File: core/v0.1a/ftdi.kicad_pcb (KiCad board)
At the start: 2 copper layers, 32 x 26 mm, 35 parts, among them J1 Conn, P1 pkl_USB_OTG, P2 UP, P3 UP, P4 UP, P5 UP, U1 93C46B-SOT-23-6, U2 FT232H, X1 12MHz

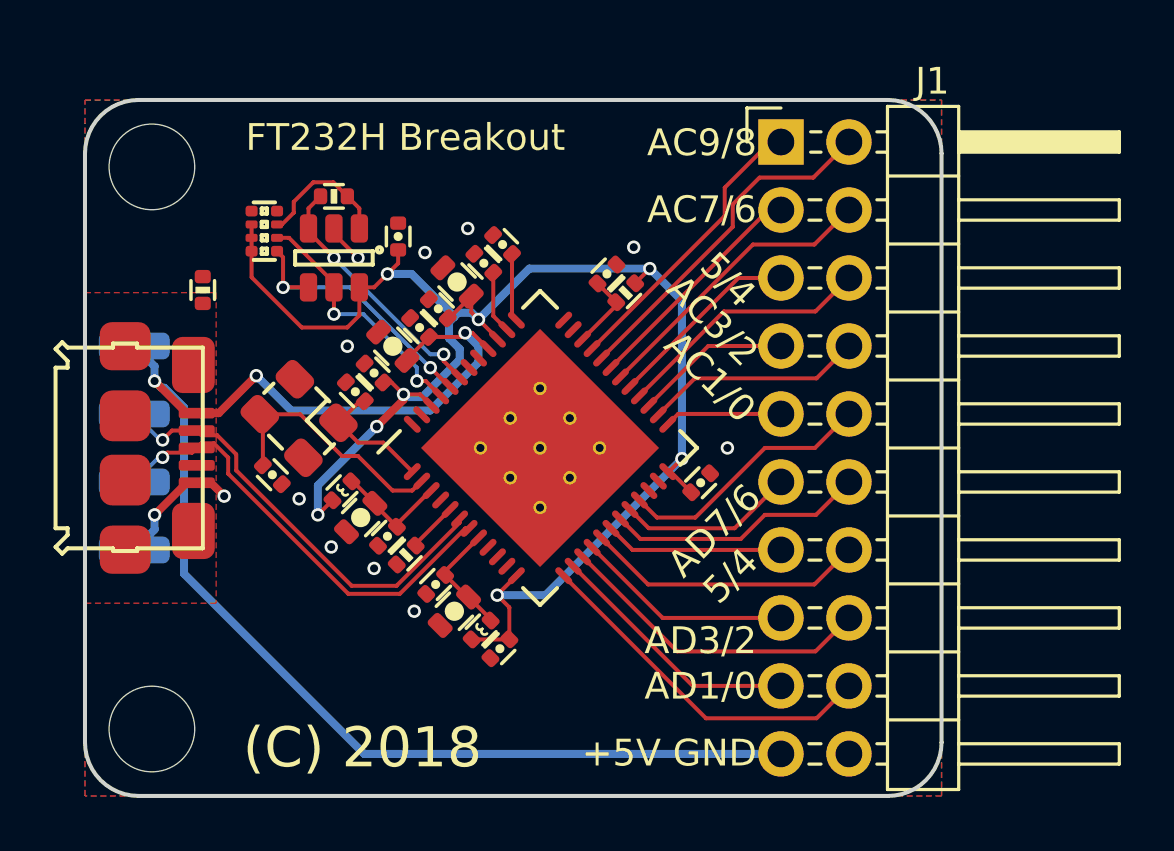
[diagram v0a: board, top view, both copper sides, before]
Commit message: Changed the ftdi breakout design to use a 50mil header.
This also decreases the width of the breakout, which will allow us to
make standard complient 0.8" wide PMOD modules using the breakout board
as a basis.
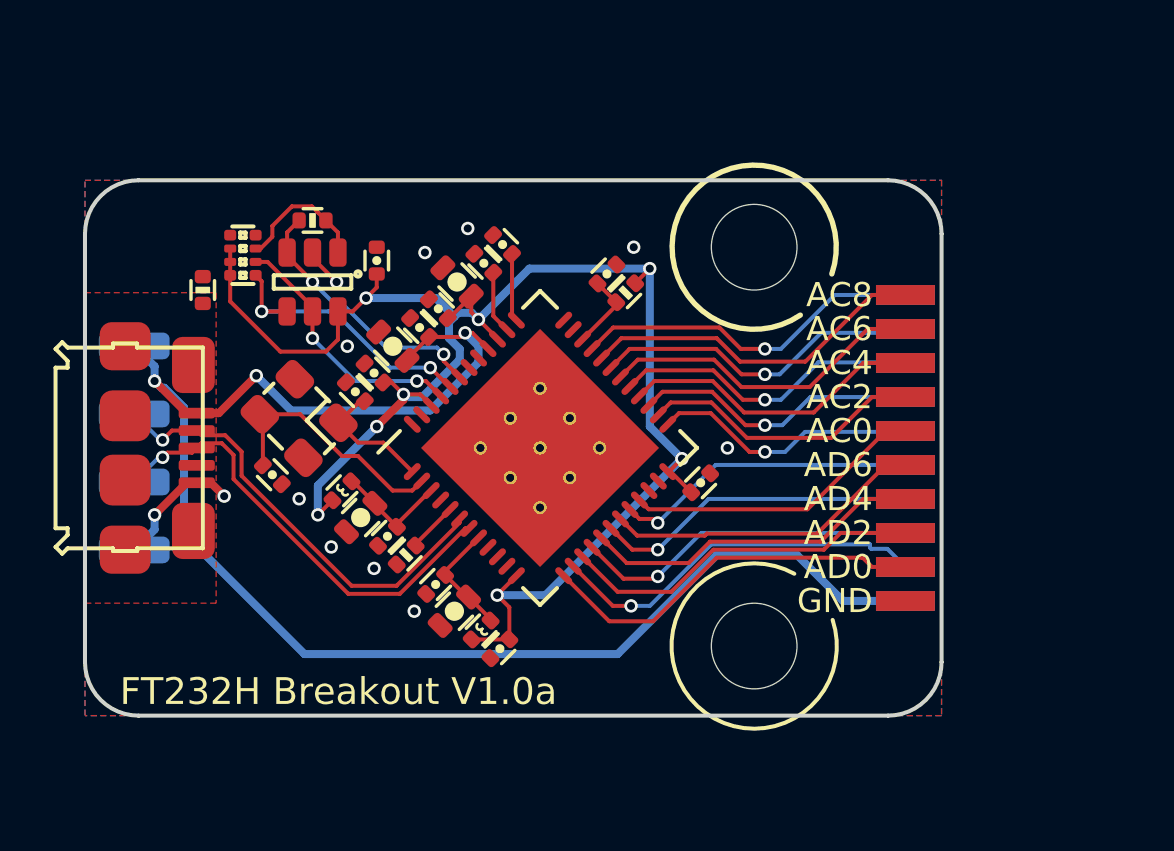
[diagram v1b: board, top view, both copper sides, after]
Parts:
- added REF**: 1b2_Logo_SilkS_5mm, pkl_logos:1b2_Logo_SilkS_5mm, B.Cu at (43.1, 47.5)
- J1: footprint Connector_PinHeader_2.54mm:PinHeader_2x10_P2.54mm_Horizontal -> pkl_samtec:FTSH-EDGE-20pin; moved to B.Cu
- moved REF** 22.7 mm to (55.0, 54.9)
- moved REF** 22.7 mm to (55.0, 40.0)
- moved J1 12.9 mm to (62.0, 47.5), turned to 270 degrees
- moved C1 1.20 mm to (40.9, 40.5)
- moved R2 1.20 mm to (35.9, 40.3)
- moved R6 1.20 mm to (38.5, 39.0)
- moved U1 1.20 mm to (38.5, 41.3)
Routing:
- net /ACBUS1: track 4.39 -> 9.98 mm, vias 0 -> 1
- net /ADBUS5: track 6.68 -> 12.1 mm, vias 0 -> 1
- net /ACBUS3: track 5.85 -> 10.7 mm, vias 0 -> 1
- net /ADBUS1: track 9.61 -> 14.4 mm, vias 0 -> 1
- net /ADBUS3: track 8.15 -> 12.9 mm, vias 0 -> 1
- net /ADBUS7: track 6.65 -> 11.4 mm, vias 0 -> 1
- net +5V: track 53.9 -> 58.4 mm
- net /ACBUS5: track 7.32 -> 11.6 mm, vias 0 -> 1
- net /ACBUS7: track 8.79 -> 12.4 mm, vias 0 -> 1
- net /ACBUS2: track 8.19 -> 10.6 mm
- net /ACBUS9: track 10.9 -> 13.2 mm, vias 0 -> 1
- net /ADBUS6: track 9.73 -> 12.0 mm
- net /ADBUS4: track 10.5 -> 12.7 mm
- net /ACBUS4: track 9.65 -> 11.4 mm
- net /ACBUS0: track 9.70 -> 11.3 mm
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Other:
- board size 32 x 26 mm -> 32 x 20 mm
- board text added: "(C)2018"
- board text added: "+5V"
- board text added: "1BitSquared"
- board text added: "AC0"
- board text added: "AC1"
- board text added: "AC2"
- board text added: "AC3"
- board text added: "AC4"
- board text added: "AC5"
- board text added: "AC6"
- board text added: "AC7"
- board text added: "AC8"
- board text added: "AC9"
- board text added: "AD0"
- board text added: "AD2"
- board text added: "AD3"
- board text added: "AD4"
- board text added: "AD5"
- board text added: "AD6"
- board text added: "AD7"
- board text added: "CC-BY-SA 4.0"
- board text added: "FT232H Breakout V1.0a"
- board text added: "GND"
- board text added: "UD+"
- board text added: "UD-"
- board text removed: "(C) 2018"
- board text removed: "+5V GND"
- board text removed: "5/4"
- board text removed: "AC1/0"
- board text removed: "AC3/2"
- board text removed: "AC7/6"
- board text removed: "AC9/8"
- board text removed: "AD1/0"
- board text removed: "AD3/2"
- board text removed: "AD7/6"
- board text removed: "FT232H Breakout"
